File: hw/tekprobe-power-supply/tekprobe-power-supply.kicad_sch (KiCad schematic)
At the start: 21 parts

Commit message: añadido reguladores y placeholder para fusibles
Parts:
- added F? (x3): ~, symbol Herranz - Protection:Fuse
- added U?: ~, Package_TO_SOT_SMD:TO-252-2, symbol Herranz - Linear Regulators:uA79M05-(TO252)
- added U?: ~, Package_TO_SOT_SMD:TO-252-2, symbol Herranz - Linear Regulators:uA78M05-(TO252)
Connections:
- net +9V: now also U?.1 (IN)
- net -9V: now also U?.1 (IN)
- net GND: now also U?.2 (GND), U?.2 (GND)
- net at C?.1, C?.1, C?.1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: now also F?.1; no longer TR?.2, TR?.3
- new net: F?.1, U?.3 (OUT) (x2)
- new net: F?.2, TR?.2, TR?.3
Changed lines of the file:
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@@
   (junction (at 205 79) (diameter 0) (color 0 0 0 0)
   )
+  (junction (at 96 153) (diameter 0) (color 0 0 0 0)
+  )
   (junction (at 212 48) (diameter 0) (color 0 0 0 0)
   )
@@
   (junction (at 96 50) (diameter 0) (color 0 0 0 0)
   )
+  (wire (pts (xy 121 50) (xy 127 50))
+    (stroke (width 0) (type default))
+  )
   (wire (pts (xy 195 79) (xy 197 79))
     (stroke (width 0) (type default))
@@
     (stroke (width 0) (type default))
   )
+  (wire (pts (xy 118 169) (xy 135 169))
+    (stroke (width 0) (type default))
+  )
   (wire (pts (xy 174 59) (xy 178 59))
     (stroke (width 0) (type default))
   )
-  (wire (pts (xy 96 50) (xy 127 50))
+  (wire (pts (xy 96 50) (xy 109 50))
     (stroke (width 0) (type default))
   )
@@
     (stroke (width 0) (type default))
   )
+  (wire (pts (xy 96 147) (xy 96 153))
+    (stroke (width 0) (type default))
+  )
   (wire (pts (xy 217 79) (xy 217 78))
     (stroke (width 0) (type default))
@@
     (stroke (width 0) (type default))
   )
+  (wire (pts (xy 96 153) (xy 122 153))
+    (stroke (width 0) (type default))
+  )
   (wire (pts (xy 158 39) (xy 166 39))
     (stroke (width 0) (type default))
@@
     (stroke (width 0) (type default))
   )
+  (wire (pts (xy 68 137) (xy 86 137))
+    (stroke (width 0) (type default))
+  )
   (wire (pts (xy 68 50) (xy 82 50))
     (stroke (width 0) (type default))
@@
     (stroke (width 0) (type default))
   )
+  (wire (pts (xy 68 169) (xy 86 169))
+    (stroke (width 0) (type default))
+  )
   (wire (pts (xy 244 31) (xy 244 39))
     (stroke (width 0) (type default))
@@
     (stroke (width 0) (type default))
   )
+  (wire (pts (xy 68 127) (xy 68 137))
+    (stroke (width 0) (type default))
+  )
   (wire (pts (xy 162 57) (xy 162 61))
     (stroke (width 0) (type default))
@@
     (stroke (width 0) (type default))
   )
+  (wire (pts (xy 68 160) (xy 68 169))
+    (stroke (width 0) (type default))
+  )
   (wire (pts (xy 178 70) (xy 234 70))
     (stroke (width 0) (type default))
@@
     (stroke (width 0) (type default))
   )
+  (wire (pts (xy 118 137) (xy 135 137))
+    (stroke (width 0) (type default))
+  )
   (wire (pts (xy 205 79) (xy 217 79))
     (stroke (width 0) (type default))
@@
   )
   (wire (pts (xy 244 39) (xy 250 39))
+    (stroke (width 0) (type default))
+  )
+  (wire (pts (xy 96 153) (xy 96 159))
     (stroke (width 0) (type default))
   )
@@
         (path "/e3022954-e773-4165-b482-c678809a5179"
           (reference "D2") (unit 1)
+        )
+      )
+    )
+  )
+  (symbol (lib_id "Herranz - Linear Regulators:uA79M05-(TO252)") (at 96 155 0) (unit 1)
+    (in_bom yes) (on_board yes) (dnp no) (fields_autoplaced)
+    (property "Reference" "U?" (at 96 172.72 0)
+      (effects (font (size 1.27 1.27)))
+    )
+    (property "Value" "~" (at 96 155 0)
+      (effects (font (size 1.27 1.27)))
+    )
+    (property "Footprint" "Package_TO_SOT_SMD:TO-252-2" (at 96 155 0)
+      (effects (font (size 1.27 1.27)) hide)
+    )
+    (property "Datasheet" "" (at 96 155 0)
+      (effects (font (size 1.27 1.27)) hide)
+    )
+    (pin "1")
+    (pin "2")
+    (pin "3")
+    (instances
+      (project "tekprobe-power-supply"
+        (path "/8cac6555-0554-4960-9c52-31b15c26c0a7"
+          (reference "U?") (unit 1)
         )
       )
@@
     )
   )
+  (symbol (lib_id "Herranz - Protection:Fuse") (at 115 50 0) (unit 1)
+    (in_bom yes) (on_board yes) (dnp no) (fields_autoplaced)
+    (property "Reference" "F?" (at 115 45.72 0)
+      (effects (font (size 1.27 1.27)))
+    )
+    (property "Value" "~" (at 115 50 0)
+      (effects (font (size 1.27 1.27)))
+    )
+    (property "Footprint" "" (at 115 50 0)
+      (effects (font (size 1.27 1.27)) hide)
+    )
+    (property "Datasheet" "" (at 115 50 0)
+      (effects (font (size 1.27 1.27)) hide)
+    )
+    (pin "1")
+    (pin "2")
+    (instances
+      (project "tekprobe-power-supply"
+        (path "/8cac6555-0554-4960-9c52-31b15c26c0a7"
+          (reference "F?") (unit 1)
+        )
+      )
+    )
+  )
   (symbol (lib_id "power:GND") (at 174 59 0) (unit 1)
     (in_bom yes) (on_board yes) (dnp no)
@@
     )
   )
+  (symbol (lib_id "power:+9V") (at 68 127 0) (unit 1)
+    (in_bom yes) (on_board yes) (dnp no) (fields_autoplaced)
+    (property "Reference" "#PWR014" (at 68 130.81 0)
+      (effects (font (size 1.27 1.27)) hide)
+    )
+    (property "Value" "+9V" (at 68 121.83 0)
+      (effects (font (size 1.27 1.27)))
+    )
+    (property "Footprint" "" (at 68 127 0)
+      (effects (font (size 1.27 1.27)) hide)
+    )
+    (property "Datasheet" "" (at 68 127 0)
+      (effects (font (size 1.27 1.27)) hide)
+    )
+    (pin "1")
+    (instances
+      (project "tekprobe-power-supply"
+        (path "/8cac6555-0554-4960-9c52-31b15c26c0a7"
+          (reference "#PWR014") (unit 1)
+        )
+      )
+      (project "TekProbe adapter"
+        (path "/e3022954-e773-4165-b482-c678809a5179"
+          (reference "#PWR0134") (unit 1)
+        )
+      )
+    )
+  )
   (symbol (lib_id "Diode:1N4148W") (at 170 39 180) (unit 1)
     (in_bom yes) (on_board yes) (dnp no) (fields_autoplaced)
@@
     )
   )
+  (symbol (lib_id "Herranz - Linear Regulators:uA78M05-(TO252)") (at 96 134 0) (unit 1)
+    (in_bom yes) (on_board yes) (dnp no) (fields_autoplaced)
+    (property "Reference" "U?" (at 96 132.08 0)
+      (effects (font (size 1.27 1.27)))
+    )
+    (property "Value" "~" (at 96 134 0)
+      (effects (font (size 1.27 1.27)))
+    )
+    (property "Footprint" "Package_TO_SOT_SMD:TO-252-2" (at 96 134 0)
+      (effects (font (size 1.27 1.27)) hide)
+    )
+    (property "Datasheet" "" (at 96 134 0)
+      (effects (font (size 1.27 1.27)) hide)
+    )
+    (pin "1")
+    (pin "2")
+    (pin "3")
+    (instances
+      (project "tekprobe-power-supply"
+        (path "/8cac6555-0554-4960-9c52-31b15c26c0a7"
+          (reference "U?") (unit 1)
+        )
+      )
+    )
+  )
   (symbol (lib_id "power:+9V") (at 223 48 0) (unit 1)
     (in_bom yes) (on_board yes) (dnp no) (fields_autoplaced)
@@
         (path "/e3022954-e773-4165-b482-c678809a5179"
           (reference "#PWR0134") (unit 1)
+        )
+      )
+    )
+  )
+  (symbol (lib_id "power:-9V") (at 68 160 0) (unit 1)
+    (in_bom yes) (on_board yes) (dnp no) (fields_autoplaced)
+    (property "Reference" "#PWR013" (at 68 163.175 0)
+      (effects (font (size 1.27 1.27)) hide)
+    )
+    (property "Value" "-9V" (at 68 155.04 0)
+      (effects (font (size 1.27 1.27)))
+    )
+    (property "Footprint" "" (at 68 160 0)
+      (effects (font (size 1.27 1.27)) hide)
+    )
+    (property "Datasheet" "" (at 68 160 0)
+      (effects (font (size 1.27 1.27)) hide)
+    )
+    (pin "1")
+    (instances
+      (project "tekprobe-power-supply"
+        (path "/8cac6555-0554-4960-9c52-31b15c26c0a7"
+          (reference "#PWR013") (unit 1)
+        )
+      )
+      (project "TekProbe adapter"
+        (path "/e3022954-e773-4165-b482-c678809a5179"
+          (reference "#PWR0137") (unit 1)
+        )
+      )
+    )
+  )
+  (symbol (lib_id "Herranz - Protection:Fuse") (at 112 169 0) (unit 1)
+    (in_bom yes) (on_board yes) (dnp no) (fields_autoplaced)
+    (property "Reference" "F?" (at 112 165.1 0)
+      (effects (font (size 1.27 1.27)))
+    )
+    (property "Value" "~" (at 112 169 0)
+      (effects (font (size 1.27 1.27)))
+    )
+    (property "Footprint" "" (at 112 169 0)
+      (effects (font (size 1.27 1.27)) hide)
+    )
+    (property "Datasheet" "" (at 112 169 0)
+      (effects (font (size 1.27 1.27)) hide)
+    )
+    (pin "1")
+    (pin "2")
+    (instances
+      (project "tekprobe-power-supply"
+        (path "/8cac6555-0554-4960-9c52-31b15c26c0a7"
+          (reference "F?") (unit 1)
+        )
+      )
+    )
+  )
+  (symbol (lib_id "Herranz - Protection:Fuse") (at 112 137 0) (unit 1)
+    (in_bom yes) (on_board yes) (dnp no) (fields_autoplaced)
+    (property "Reference" "F?" (at 112 133.35 0)
+      (effects (font (size 1.27 1.27)))
+    )
+    (property "Value" "~" (at 112 137 0)
+      (effects (font (size 1.27 1.27)))
+    )
+    (property "Footprint" "" (at 112 137 0)
+      (effects (font (size 1.27 1.27)) hide)
+    )
+    (property "Datasheet" "" (at 112 137 0)
+      (effects (font (size 1.27 1.27)) hide)
+    )
+    (pin "1")
+    (pin "2")
+    (instances
+      (project "tekprobe-power-supply"
+        (path "/8cac6555-0554-4960-9c52-31b15c26c0a7"
+          (reference "F?") (unit 1)
         )
       )
@@
         )
       )
+    )
+  )
+  (symbol (lib_id "power:GND") (at 122 153 0) (unit 1)
+    (in_bom yes) (on_board yes) (dnp no)
+    (property "Reference" "#PWR012" (at 122 159.35 0)
+      (effects (font (size 1.27 1.27)) hide)
+    )
+    (property "Value" "GND" (at 122 157 0)
+      (effects (font (size 1.27 1.27)))
+    )
+    (property "Footprint" "" (at 122 153 0)
+      (effects (font (size 1.27 1.27)) hide)
+    )
+    (property "Datasheet" "" (at 122 153 0)
+      (effects (font (size 1.27 1.27)) hide)
+    )
+    (pin "1")
+    (instances
+      (project "tekprobe-power-supply"
+        (path "/8cac6555-0554-4960-9c52-31b15c26c0a7"
+          (reference "#PWR012") (unit 1)
+        )
+      )
+      (project "TekProbe adapter"
+        (path "/e3022954-e773-4165-b482-c678809a5179"
+          (reference "#PWR0138") (unit 1)
+        )
+      )

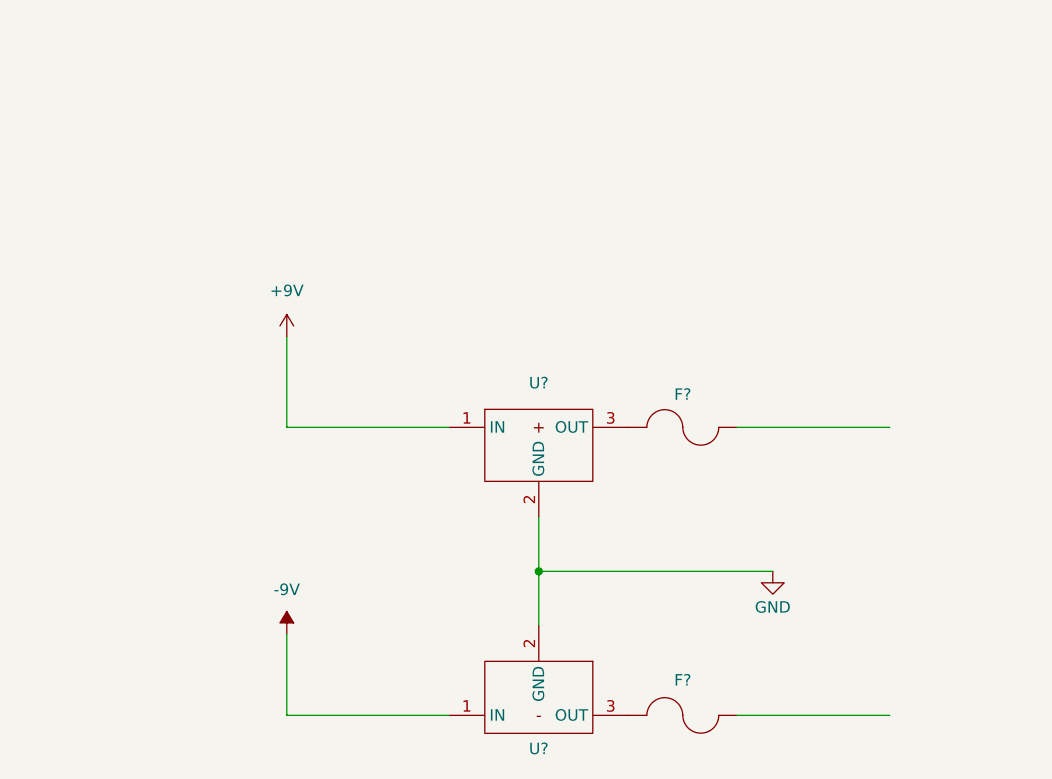
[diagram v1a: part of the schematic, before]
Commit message: fix 5v power supply
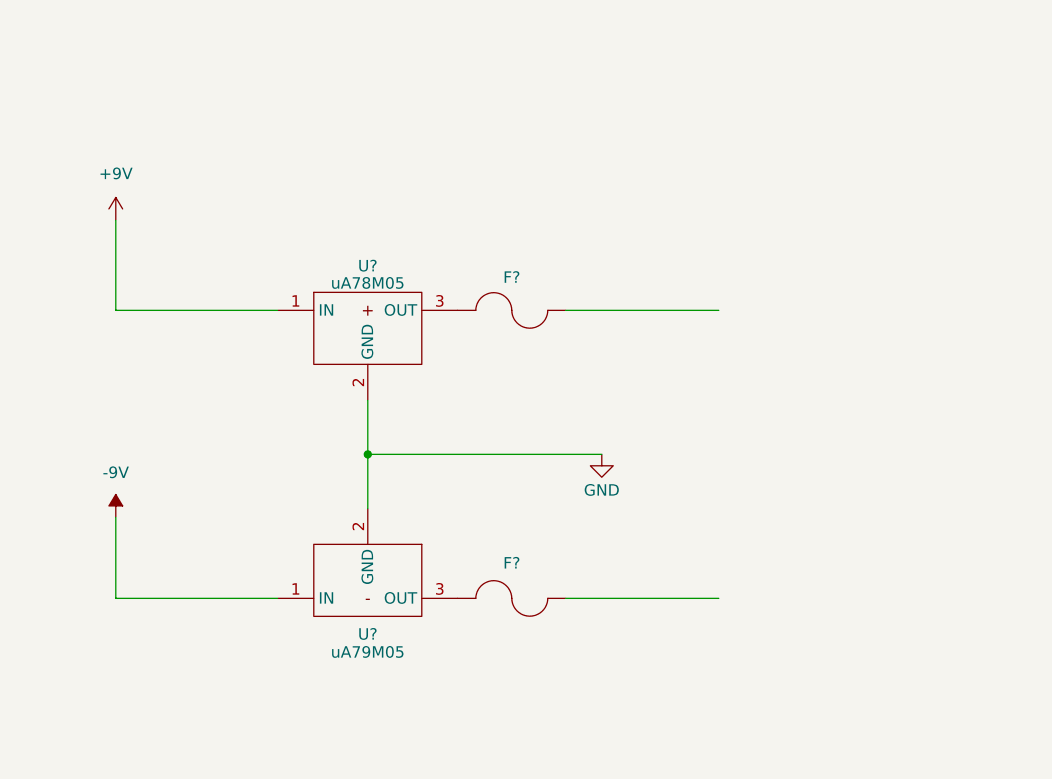
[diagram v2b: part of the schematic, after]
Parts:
- U?: value ~ -> uA79M05
- U?: value ~ -> uA78M05
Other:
- moved on the sheet: F?, U?

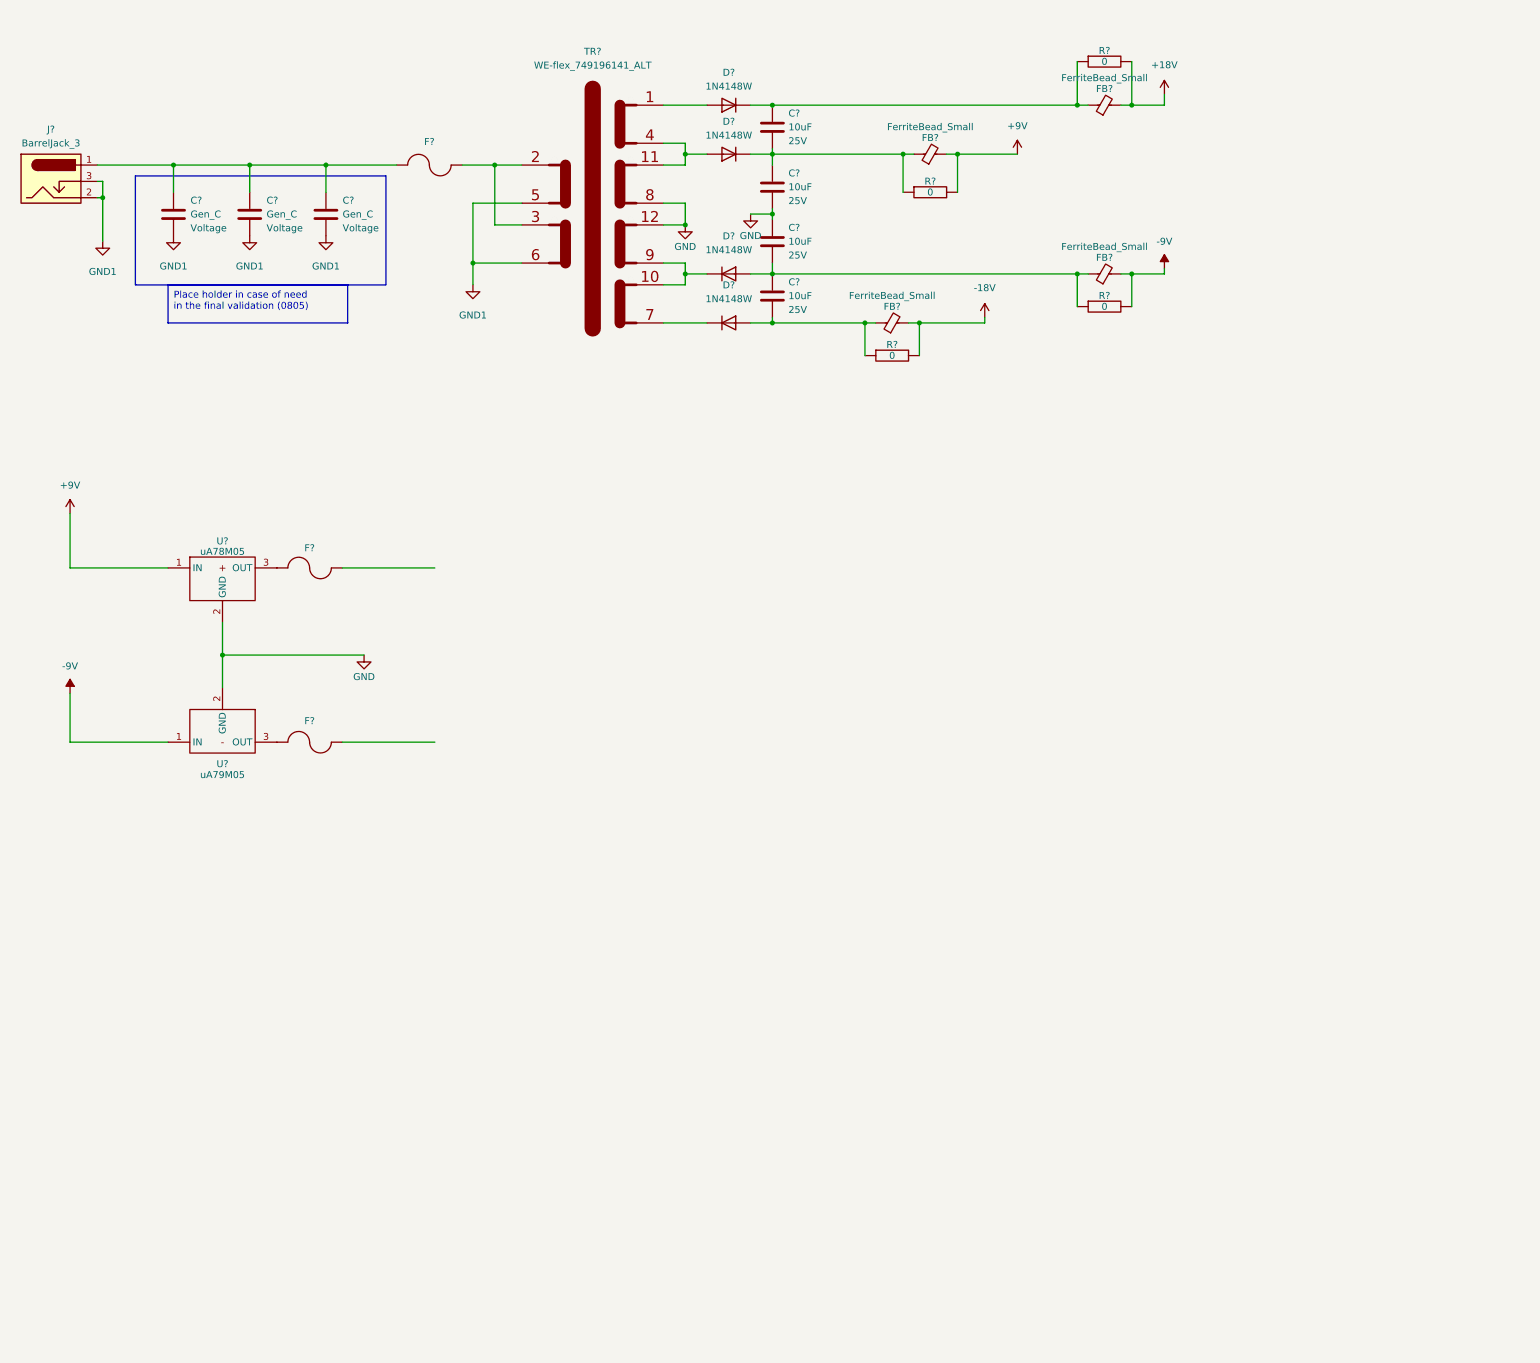
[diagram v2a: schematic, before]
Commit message: eliminado el lm317, buscando otras soluciones
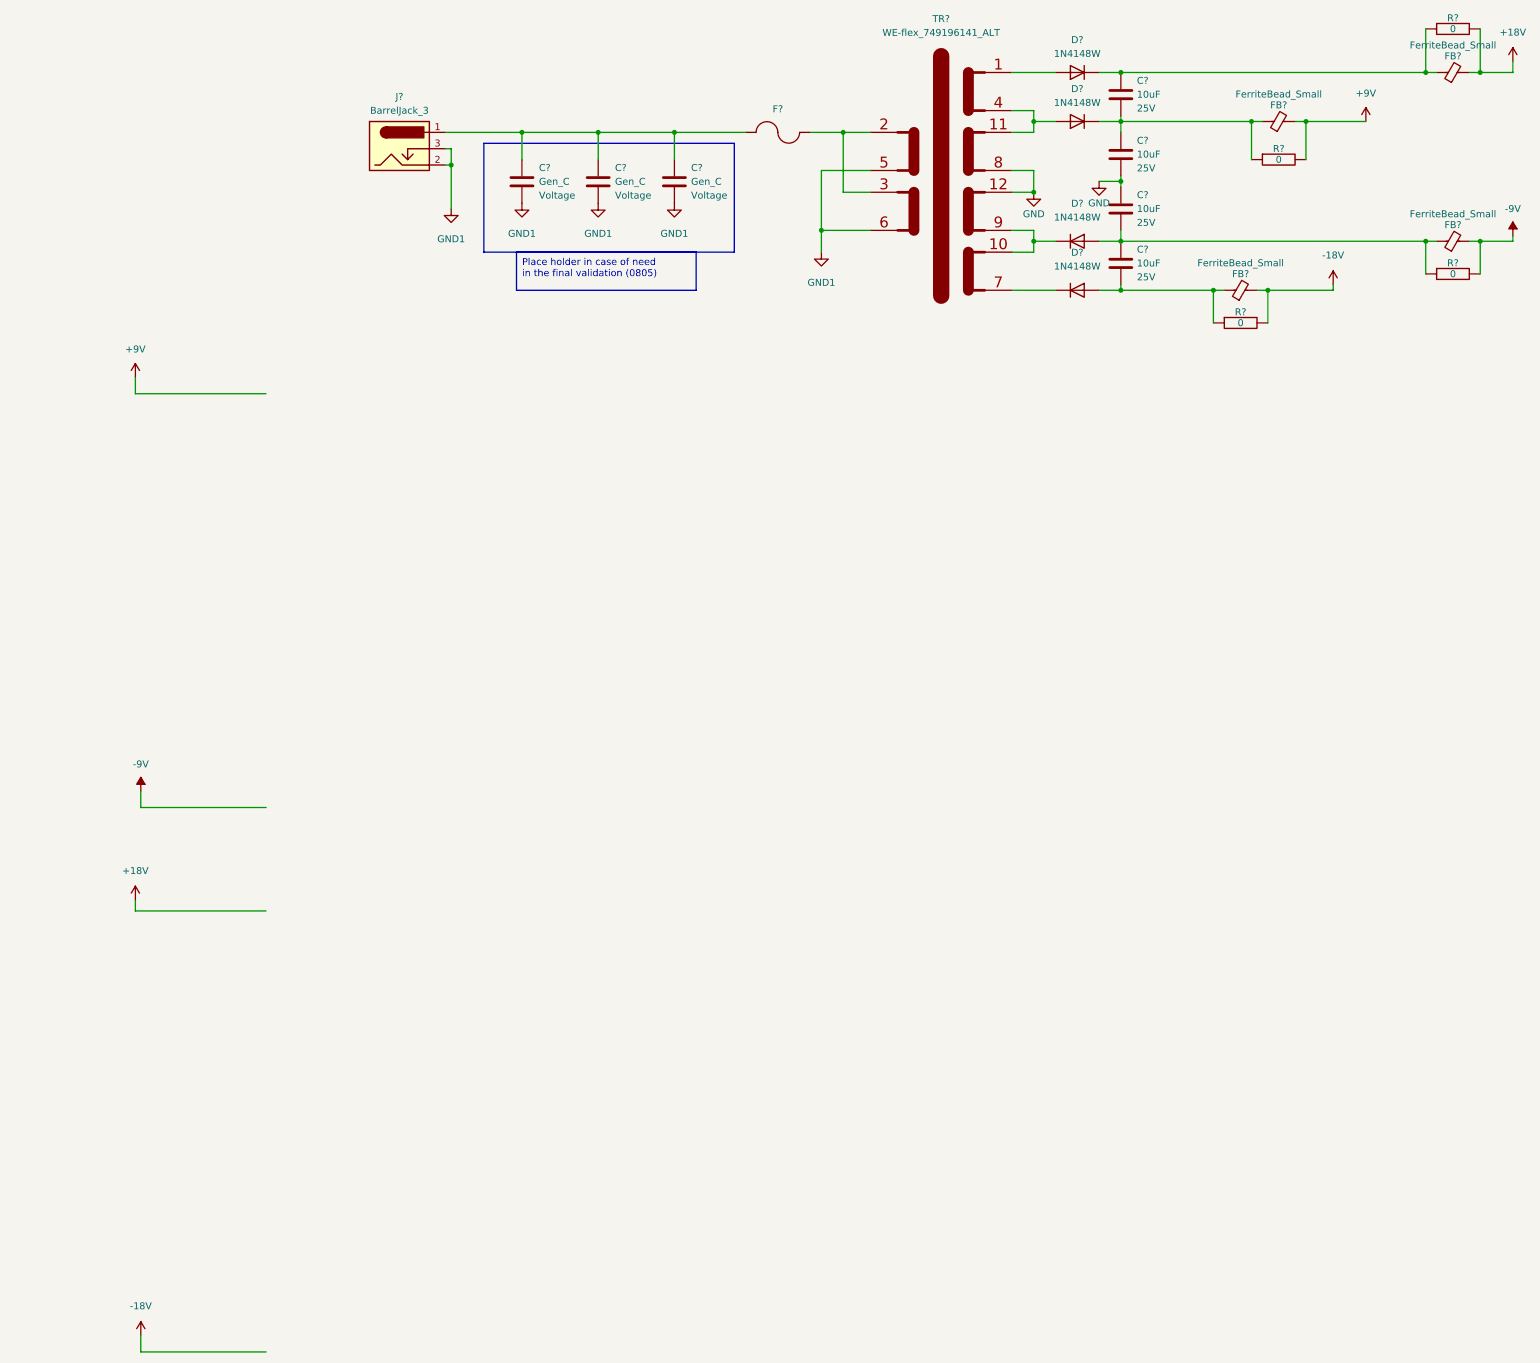
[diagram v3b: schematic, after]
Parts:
- removed F? (x2): ~, symbol Herranz - Protection:Fuse
- removed U?: uA79M05, Package_TO_SOT_SMD:TO-252-2, symbol Herranz - Linear Regulators:uA79M05-(TO252)
- removed U?: uA78M05, Package_TO_SOT_SMD:TO-252-2, symbol Herranz - Linear Regulators:uA78M05-(TO252)
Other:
- moved on the sheet: C?, D?, F?, FB?, J?, R?, TR?
